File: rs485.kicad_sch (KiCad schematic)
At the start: 60 parts, among them J10 Conn_02x01, J11 Conn_02x01, J12 Conn_02x01, J13 Conn_02x01, J14 Conn_02x01, J15 Conn_02x01, J8 Screw_Terminal_01x03, J9 Screw_Terminal_01x03, U10 CRE1S0505SC, U11 ISO308xDWR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

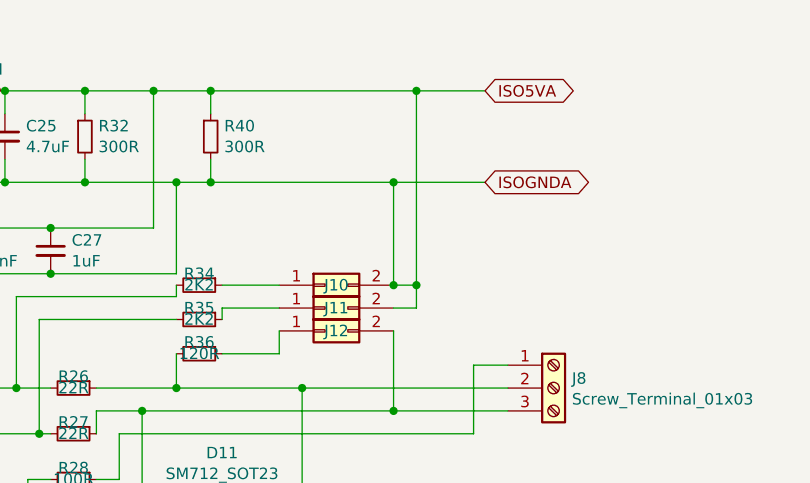
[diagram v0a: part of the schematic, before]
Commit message: Fix incorrect connection between ISO5VA and ISOGNDA (fix associated planes in pcb)
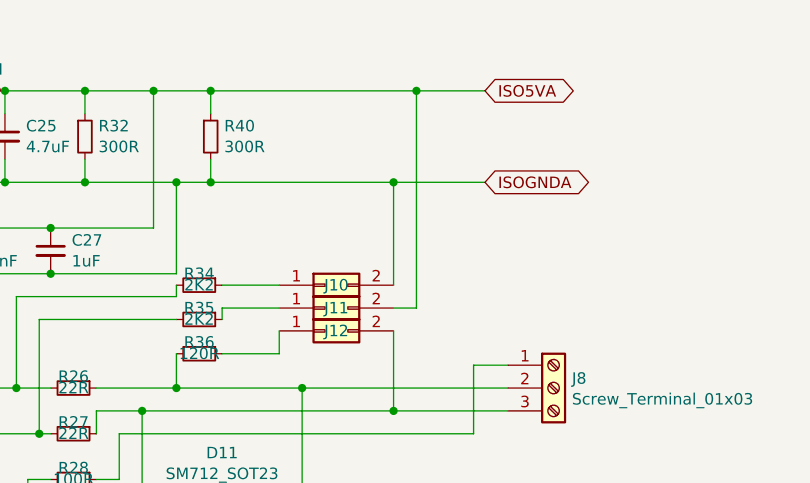
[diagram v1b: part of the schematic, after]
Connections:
- net ISO5VA: no longer C23.2, C25.2, C27.2, D11.3 (common), J10.2 (Pin_2), R28.2, R32.2, R40.2, U8.3 (-VOUT), U9.15 (GND2), U9.9 (GND2)
- new net ISOGNDA: C23.2, C25.2, C27.2, D11.3 (common), J10.2 (Pin_2), R28.2, R32.2, R40.2, U8.3 (-VOUT), U9.15 (GND2), U9.9 (GND2)
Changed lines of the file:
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@@
   (junction (at 58.42 48.26) (diameter 0) (color 0 0 0 0)
   )
-  (junction (at 232.41 50.8) (diameter 0) (color 0 0 0 0)
-  )
   (junction (at 212.09 110.49) (diameter 0) (color 0 0 0 0)
   )
@@
   (junction (at 182.88 44.45) (diameter 0) (color 0 0 0 0)
   )
-  (junction (at 234.95 50.8) (diameter 0) (color 0 0 0 0)
-  )
   (junction (at 212.09 100.33) (diameter 0) (color 0 0 0 0)
   )
@@
     (stroke (width 0) (type default) (color 0 0 0 0))
   )
-  (wire (pts (xy 234.95 50.8) (xy 234.95 29.21))
+  (wire (pts (xy 234.95 29.21) (xy 234.95 53.34))
     (stroke (width 0) (type default) (color 0 0 0 0))
   )
@@
     (stroke (width 0) (type default) (color 0 0 0 0))
   )
-  (wire (pts (xy 234.95 53.34) (xy 234.95 50.8))
-    (stroke (width 0) (type default) (color 0 0 0 0))
-  )
   (wire (pts (xy 201.93 143.51) (xy 201.93 138.43))
     (stroke (width 0) (type default) (color 0 0 0 0))
@@
     (stroke (width 0) (type default) (color 0 0 0 0))
   )
-  (wire (pts (xy 232.41 50.8) (xy 234.95 50.8))
-    (stroke (width 0) (type default) (color 0 0 0 0))
-  )
